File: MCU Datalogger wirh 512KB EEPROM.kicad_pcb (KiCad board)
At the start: 2 copper layers, 56.3 x 48.7 mm, 30 parts, among them IC1 ATMEGA328P-AU, J1 Conn_01x04_Pin, J2 Conn_01x04_Pin, J3 Conn_01x09_Pin, J4 Conn_02x03_Odd_Even, U1 24LC1025, U2 24LC1025, U3 DS1137S+, Y1 16 MHz, Y2 32.768 KHz

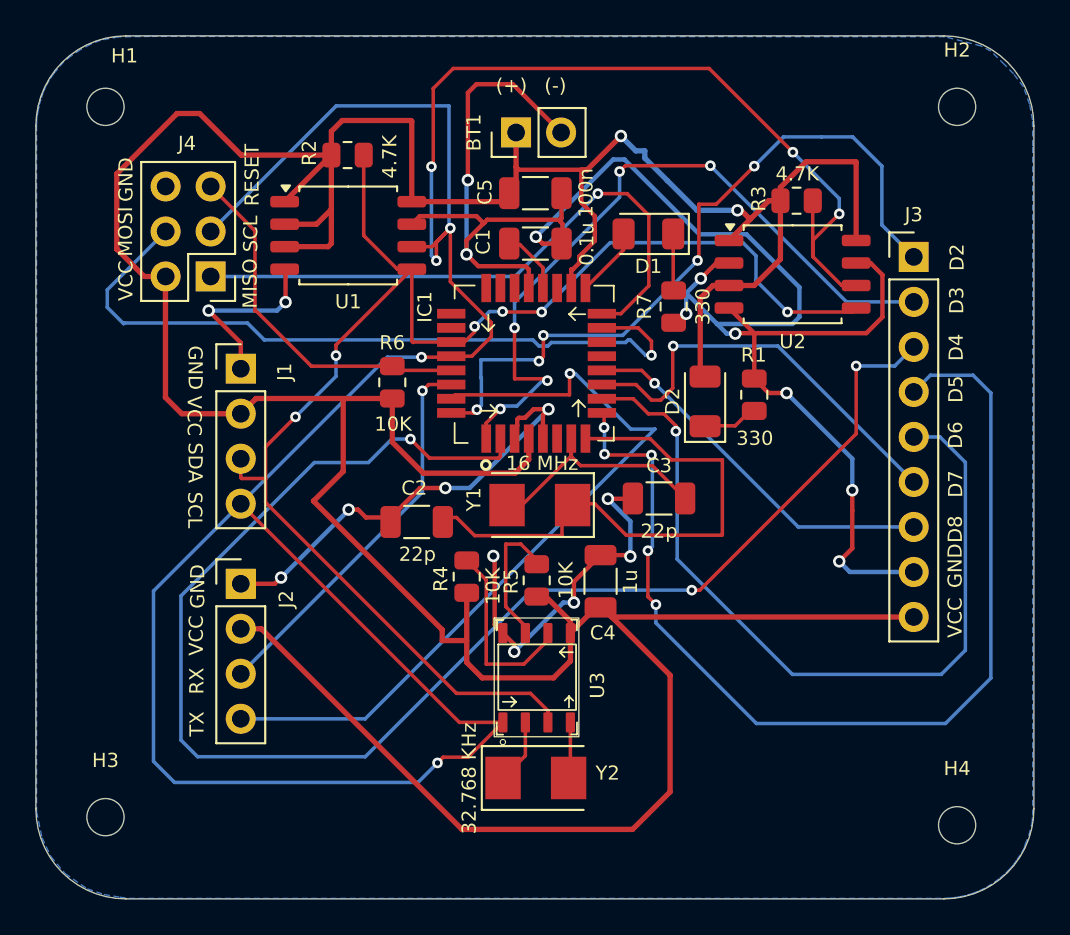
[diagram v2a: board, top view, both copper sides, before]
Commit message: Included the names of ICs to the front silkscreen.
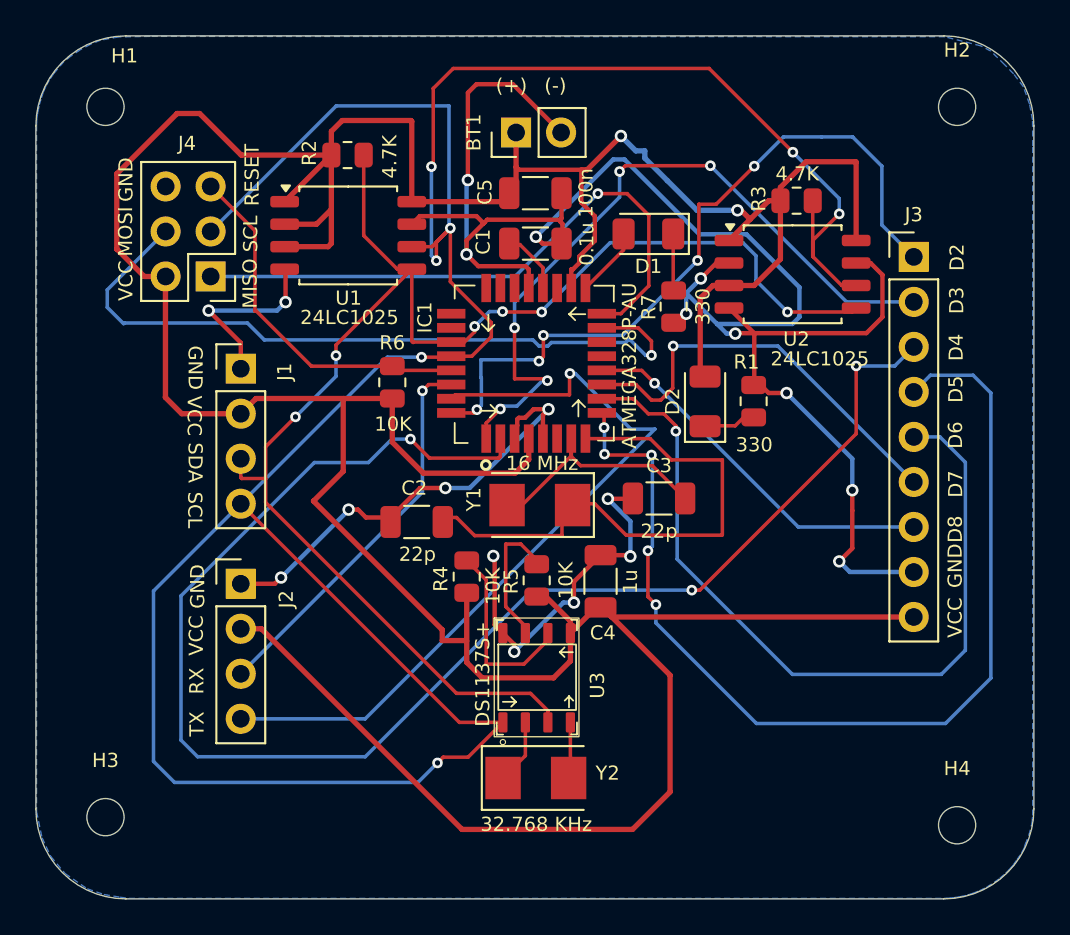
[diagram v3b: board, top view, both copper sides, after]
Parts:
- moved R1 0.37 mm to (148.2, 95.3)
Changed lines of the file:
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@@
 		(tags "SOIC SO P-SOP SOP SOP-8 SO SO-8 8S2 S2AE/F K04-056 CASE-751BE SO8W 8-Pin-SOIC PSA W8-2 W8-4 W8MS-1")
 		(property "Reference" "U2"
-			(at 0 3.8 0)
+			(at 0.2164 3.6589 0)
 			(layer "F.SilkS")
 			(effects
@@
 		)
 		(property "Value" "24LC1025"
-			(at 0 3.6 0)
-			(layer "F.Fab")
+			(at 1.5372 4.7765 0)
+			(layer "F.SilkS")
 			(effects
 				(font
-					(size 1 1)
+					(size 0.8 0.8)
 					(thickness 0.15)
 				)
@@
 		(tags "resistor")
 		(property "Reference" "R7"
-			(at 0 -1.65 90)
+			(at -0.0305 -1.4023 90)
 			(layer "F.SilkS")
 			(effects
@@
 		)
 		(property "Value" "32.768 KHz"
-			(at -3.7619 0.0243 90)
+			(at 0.0227 2.6151 180)
 			(layer "F.SilkS")
 			(effects
@@
 		(tags "SOIC SO P-SOP SOP SOP-8 SO SO-8 8S2 S2AE/F K04-056 CASE-751BE SO8W 8-Pin-SOIC PSA W8-2 W8-4 W8MS-1")
 		(property "Reference" "U1"
-			(at 0 3.74 0)
+			(at 0.0184 3.5375 0)
 			(layer "F.SilkS")
 			(effects
@@
 		)
 		(property "Value" "24LC1025"
-			(at 0 3.6 0)
-			(layer "F.Fab")
+			(at 0.0692 4.6297 0)
+			(layer "F.SilkS")
 			(effects
 				(font
-					(size 1 1)
+					(size 0.8 0.8)
 					(thickness 0.15)
 				)
@@
 	(footprint "Resistor_SMD:R_0805_2012Metric"
 		(layer "F.Cu")
-		(at 148.2685 94.9621 90)
+		(at 148.2344 95.3262 90)
 		(descr "Resistor SMD 0805 (2012 Metric), square (rectangular) end terminal, IPC-7351 nominal, (Body size source: IPC-SM-782 page 72, https://www.pcb-3d.com/wordpress/wp-content/uploads/ipc-sm-782a_amendment_1_and_2.pdf), generated with kicad-footprint-generator")
 		(tags "resistor")
 		(property "Reference" "R1"
-			(at 2.2421 -0.0285 0)
+			(at 2.2098 -0.4064 0)
 			(layer "F.SilkS")
 			(effects
@@
 		)
 		(property "Value" "DS1137S+"
-			(at 1.16 -8.4 0)
+			(at -1.1399 -2.731 90)
 			(unlocked yes)
-			(layer "F.Fab")
+			(layer "F.SilkS")
 			(effects
 				(font
-					(size 1 1)
+					(size 0.8 0.8)
 					(thickness 0.15)
 				)
@@
 		(at 133.1435 97.4371)
 		(property "Reference" "IC1"
-			(at -3.4635 -7.4271 90)
+			(at -3.4635 -6.8353 90)
 			(unlocked yes)
 			(layer "F.SilkS")
@@
 		)
 		(property "Value" "ATMEGA328P-AU"
-			(at 2.91 -11.98 0)
+			(at 8.0805 -4.1175 90)
 			(unlocked yes)
-			(layer "F.Fab")
+			(layer "F.SilkS")
 			(effects
 				(font
-					(size 1 1)
+					(size 0.8 0.8)
 					(thickness 0.15)
 				)
@@
 	)
 	(segment
+		(start 149.0828 94.8639)
+		(end 148.6326 94.4137)
+		(width 0.25)
+		(layer "F.Cu")
+		(net 1)
+	)
+	(segment
 		(start 134.7251 109.0512)
 		(end 134.0835 108.4096)
@@
 	)
 	(segment
-		(start 148.2685 91.4921)
-		(end 148.2685 94.0496)
-		(width 0.25)
-		(layer "F.Cu")
-		(net 1)
-	)
-	(segment
 		(start 155.5023 90.5777)
 		(end 154.5943 91.4857)
@@
 	)
 	(segment
-		(start 149.0828 94.8639)
-		(end 148.2685 94.0496)
-		(width 0.25)
-		(layer "F.Cu")
-		(net 1)
-	)
-	(segment
 		(start 148.2749 91.4857)
 		(end 148.2685 91.4921)
@@
 	)
 	(segment
+		(start 148.2685 91.4921)
+		(end 148.2685 94.3796)
+		(width 0.25)
+		(layer "F.Cu")
+		(net 1)
+	)
+	(segment
 		(start 137.3159 85.1865)
 		(end 137.4435 85.3141)
@@
 	)
 	(segment
+		(start 148.2685 94.3796)
+		(end 148.2344 94.4137)
+		(width 0.25)
+		(layer "F.Cu")
+		(net 1)
+	)
+	(segment
 		(start 134.6459 77.4395)
 		(end 132.5915 77.4395)
@@
 	)
 	(segment
-		(start 150.0921 94.8639)
-		(end 149.0828 94.8639)
-		(width 0.25)
-		(layer "F.Cu")
-		(net 1)
-	)
-	(segment
 		(start 127.745 102.14)
 		(end 127.745 101.8856)
@@
 	)
 	(segment
+		(start 148.6326 94.4137)
+		(end 148.2344 94.4137)
+		(width 0.25)
+		(layer "F.Cu")
+		(net 1)
+	)
+	(segment
 		(start 145.2534 88.3996)
 		(end 146.1259 87.5271)
@@
 	)
 	(segment
+		(start 150.0921 94.8639)
+		(end 149.0828 94.8639)
+		(width 0.25)
+		(layer "F.Cu")
+		(net 1)
+	)
+	(segment
 		(start 133.6195 107.9456)
 		(end 133.6195 104.1347)
@@
 	)
 	(segment
-		(start 145.4935 96.7371)
-		(end 145.5185 96.7121)
+		(start 147.6669 96.2387)
+		(end 148.2344 96.2387)
 		(width 0.2)
 		(layer "F.Cu")
@@
 	(segment
 		(start 147.1935 96.7121)
-		(end 148.031 95.8746)
+		(end 147.6669 96.2387)
 		(width 0.2)
 		(layer "F.Cu")
@@
 	)
 	(segment
-		(start 145.5185 96.7121)
-		(end 147.1935 96.7121)
+		(start 145.4935 96.7371)
+		(end 145.5185 96.7121)
 		(width 0.2)
 		(layer "F.Cu")
@@
 	)
 	(segment
-		(start 148.031 95.8746)
-		(end 148.2685 95.8746)
+		(start 145.5185 96.7121)
+		(end 147.1935 96.7121)
 		(width 0.2)
 		(layer "F.Cu")
